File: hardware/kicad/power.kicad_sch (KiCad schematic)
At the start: 15 parts, among them U10 TLV75533PDBVR, U11 REF3330AIDBZR

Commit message: Clean KiCad 9 root-hierarchy ERC in the generator; add outline DRC to kicad_check
- make_design.py: place symbols, wires, labels and no-connects on the 1.27 mm grid
  (endpoint_off_grid 872 -> 0); add PWR_FLAG on +5V_FUSED and GND, which are fed
  only from off-board USB through passive Pico socket contacts and fuse F1
  (power_pin_not_driven 2 -> 0); generate 74HC4067 Y/Z as passive analog-switch
  terminals instead of bidirectional.
- kicad_check.py: every remaining ERC item needs a reason, endpoint_off_grid and
  lib_symbol_* must be 0, outline-board DRC error count recorded and gated.
- validate.py: exclude '#' power/flag symbols from the physical instance inventory.

Refs #11

Co-Authored-By: Claude Opus 5.5 <noreply@anthropic.com>
Claude-Session: https://claude.ai/code/session_018oLpisCWqu84U1dDpzLDZ4
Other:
- moved on the sheet: C30, C31, C32, C33, F1, R30, TP40, TP41, TP42, TP43, TP44, TP45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

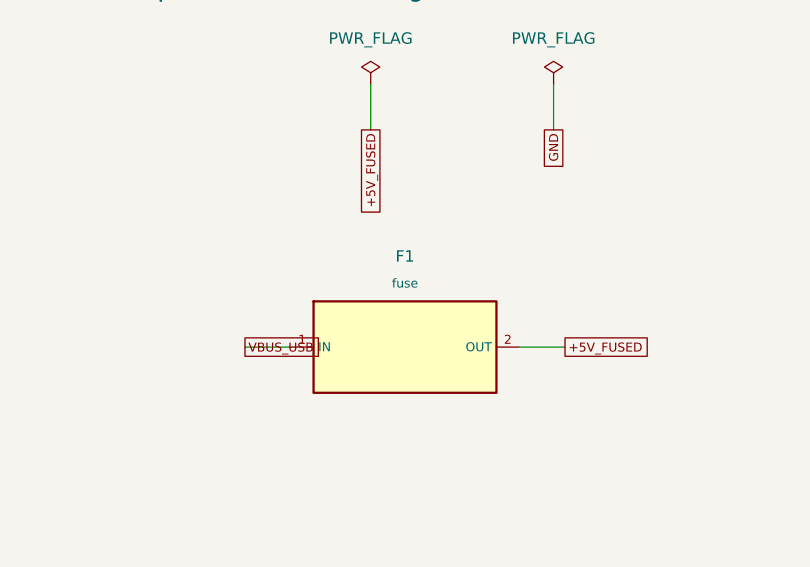
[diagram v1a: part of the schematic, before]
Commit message: Generator integrator: apply G01/G02/G08 evidence deltas, candidate footprints (#13)
Applies the cited deltas from #3 (g01-delta.json), #6 (g02-delta.json) and #9
(g08-delta.json) to scripts/make_design.py and catalog/*.json, the only topic
allowed to touch those files.

- G01: record the display-header notes and the R16/R88 backlight default-on
  conflict as a pending_g01_changes proposal only; J30/J31 nets are unchanged,
  per the G01 header-net rule. Documented in the power narrative source too.
- G02: apply the NKK range-switch numeric terminal map (C->3, M->2 vendor
  facts; L->1/H->4 marked OPEN pending panel orientation) and add the
  resolved mechanical facts/open-questions for range, jack, button, display,
  pico-h, socket20 and header20.
- G08: add mpn/jlc_code (with citation, listing_not_allocation) for every
  specification-only candidate that had a source URL and checked date; skip
  r249k/socket20/header20, which have no located citation.
- Fix scripts/fetch_sources.py to download into the gitignored
  reference/downloads/ and write its local fetch log there instead of the
  tracked reference/downloaded/ and reports/source-fetch-local.json.
- Regenerate KiCad sheets/netlist/BOM/MDX/offline HTML; write
  design/evidence/INTEGRATION.md with the footprint-coverage summary and the
  applied/skipped delta table.

validate.py 72/72, kicad_check.py (ERC 0 unexplained, DRC 0, parity PASS,
224/134, 0 differences), test_firmware.py and analyze.py all pass, matching
the pre-existing baseline exactly. G01/G02/G08 stay OPEN.

Co-Authored-By: Claude Sonnet 5 <noreply@anthropic.com>
Claude-Session: https://claude.ai/code/session_018oLpisCWqu84U1dDpzLDZ4
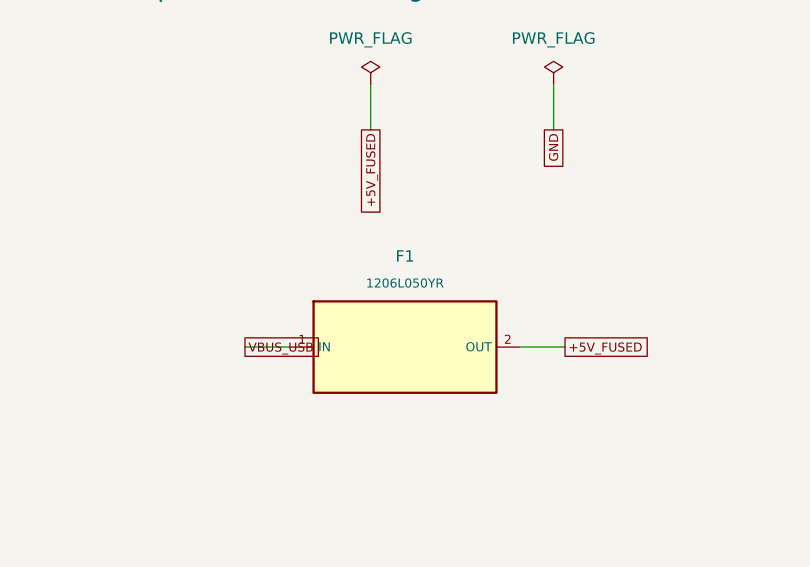
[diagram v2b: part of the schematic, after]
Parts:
- F1: value fuse -> 1206L050YR
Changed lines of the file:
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@@
 (symbol (lib_id "ZudoScope10:fuse") (at 44.45 54.61 0) (unit 1) (in_bom yes) (on_board yes) (dnp no)
 (property "Reference" "F1" (at 44.45 44.53 0) (effects (font (size 1.27 1.27))))
-(property "Value" "fuse" (at 44.45 47.53 0) (effects (font (size 1.0 1.0))))
+(property "Value" "1206L050YR" (at 44.45 47.53 0) (effects (font (size 1.0 1.0))))
 (property "Footprint" "" (at 44.45 54.61 0) (effects (font (size 1.0 1.0)) hide))
 (property "Datasheet" "" (at 44.45 54.61 0) (effects (font (size 1.0 1.0)) hide))
